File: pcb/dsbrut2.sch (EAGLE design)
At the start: 14 parts, among them IC1 4175D, IC2 74HC125D, IC3 MEGA8-AI

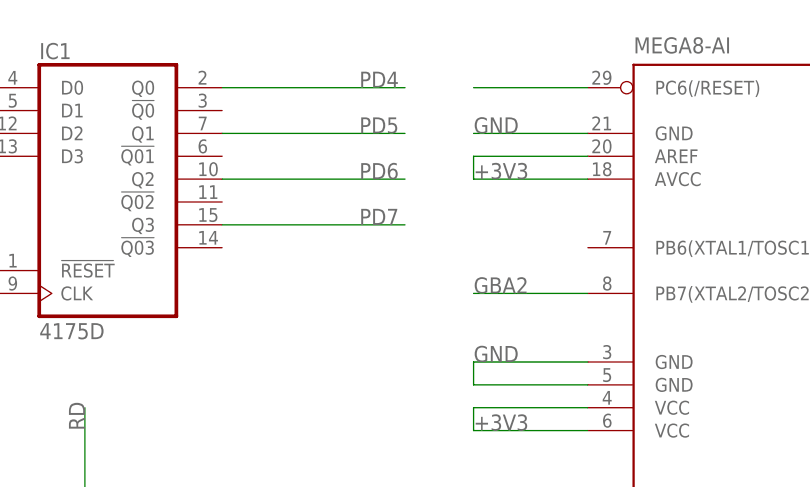
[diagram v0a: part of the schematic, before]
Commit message: added crystal, jumper bridge for gba2
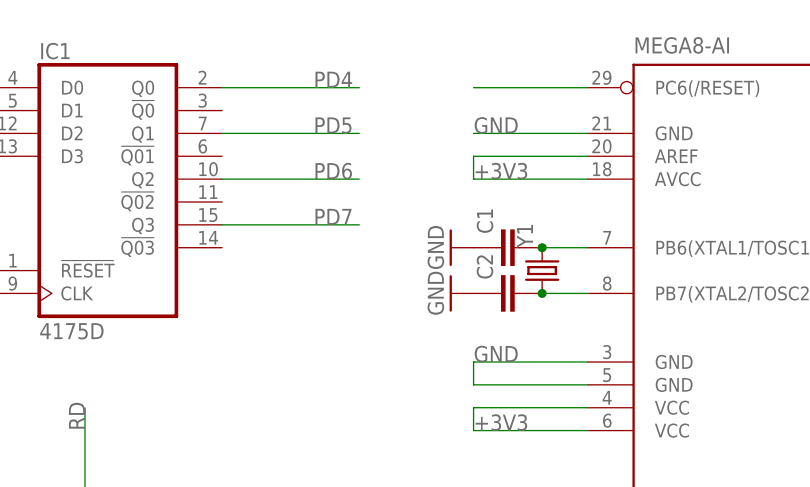
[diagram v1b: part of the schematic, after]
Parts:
- added C1, C2: (no value), rcl:C-EUC0603K
- added Y1: (no value), SparkFun-FreqCtrl:CRYSTAL5X3
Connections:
- new net N$3: C1.2, IC3.PB6(XTAL1/TOSC1), Y1.2
- new net PB7: C2.2, IC3.PB7(XTAL2/TOSC2), Y1.1
- net GBA2: no longer IC3.PB7(XTAL2/TOSC2)
- net GND: now also C1.1, C2.1
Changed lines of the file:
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@@
 <grid distance="0.1" unitdist="inch" unit="inch" style="lines" multiple="1" display="no" altdistance="0.01" altunitdist="inch" altunit="inch"/>
 <layers>
-<layer number="1" name="Top" color="4" fill="1" visible="yes" active="no"/>
-<layer number="16" name="Bottom" color="1" fill="1" visible="yes" active="no"/>
-<layer number="17" name="Pads" color="2" fill="1" visible="yes" active="no"/>
-<layer number="18" name="Vias" color="2" fill="1" visible="yes" active="no"/>
-<layer number="19" name="Unrouted" color="6" fill="1" visible="yes" active="no"/>
-<layer number="20" name="Dimension" color="15" fill="1" visible="yes" active="no"/>
-<layer number="21" name="tPlace" color="7" fill="1" visible="yes" active="no"/>
-<layer number="22" name="bPlace" color="7" fill="1" visible="yes" active="no"/>
-<layer number="23" name="tOrigins" color="15" fill="1" visible="yes" active="no"/>
-<layer number="24" name="bOrigins" color="15" fill="1" visible="yes" active="no"/>
-<layer number="25" name="tNames" color="7" fill="1" visible="yes" active="no"/>
-<layer number="26" name="bNames" color="7" fill="1" visible="yes" active="no"/>
-<layer number="27" name="tValues" color="7" fill="1" visible="yes" active="no"/>
-<layer number="28" name="bValues" color="7" fill="1" visible="yes" active="no"/>
+<layer number="1" name="Top" color="4" fill="1" visible="no" active="no"/>
+<layer number="16" name="Bottom" color="1" fill="1" visible="no" active="no"/>
+<layer number="17" name="Pads" color="2" fill="1" visible="no" active="no"/>
+<layer number="18" name="Vias" color="2" fill="1" visible="no" active="no"/>
+<layer number="19" name="Unrouted" color="6" fill="1" visible="no" active="no"/>
+<layer number="20" name="Dimension" color="15" fill="1" visible="no" active="no"/>
+<layer number="21" name="tPlace" color="7" fill="1" visible="no" active="no"/>
+<layer number="22" name="bPlace" color="7" fill="1" visible="no" active="no"/>
+<layer number="23" name="tOrigins" color="15" fill="1" visible="no" active="no"/>
+<layer number="24" name="bOrigins" color="15" fill="1" visible="no" active="no"/>
+<layer number="25" name="tNames" color="7" fill="1" visible="no" active="no"/>
+<layer number="26" name="bNames" color="7" fill="1" visible="no" active="no"/>
+<layer number="27" name="tValues" color="7" fill="1" visible="no" active="no"/>
+<layer number="28" name="bValues" color="7" fill="1" visible="no" active="no"/>
 <layer number="29" name="tStop" color="7" fill="3" visible="no" active="no"/>
 <layer number="30" name="bStop" color="7" fill="6" visible="no" active="no"/>
@@
 <layer number="35" name="tGlue" color="7" fill="4" visible="no" active="no"/>
 <layer number="36" name="bGlue" color="7" fill="5" visible="no" active="no"/>
-<layer number="37" name="tTest" color="7" fill="1" visible="yes" active="no"/>
-<layer number="38" name="bTest" color="7" fill="1" visible="yes" active="no"/>
+<layer number="37" name="tTest" color="7" fill="1" visible="no" active="no"/>
+<layer number="38" name="bTest" color="7" fill="1" visible="no" active="no"/>
 <layer number="39" name="tKeepout" color="4" fill="11" visible="no" active="no"/>
 <layer number="40" name="bKeepout" color="1" fill="11" visible="no" active="no"/>
@@
 <layer number="44" name="Drills" color="7" fill="1" visible="no" active="no"/>
 <layer number="45" name="Holes" color="7" fill="1" visible="no" active="no"/>
-<layer number="46" name="Milling" color="3" fill="1" visible="yes" active="no"/>
-<layer number="47" name="Measures" color="7" fill="1" visible="yes" active="no"/>
-<layer number="48" name="Document" color="7" fill="1" visible="yes" active="no"/>
-<layer number="49" name="Reference" color="7" fill="1" visible="yes" active="no"/>
-<layer number="50" name="dxf" color="7" fill="1" visible="yes" active="no"/>
-<layer number="51" name="tDocu" color="7" fill="1" visible="yes" active="no"/>
-<layer number="52" name="bDocu" color="7" fill="1" visible="yes" active="no"/>
-<layer number="53" name="tGND_GNDA" color="7" fill="9" visible="yes" active="no"/>
-<layer number="54" name="bGND_GNDA" color="1" fill="9" visible="yes" active="no"/>
-<layer number="56" name="wert" color="7" fill="1" visible="yes" active="no"/>
+<layer number="46" name="Milling" color="3" fill="1" visible="no" active="no"/>
+<layer number="47" name="Measures" color="7" fill="1" visible="no" active="no"/>
+<layer number="48" name="Document" color="7" fill="1" visible="no" active="no"/>
+<layer number="49" name="Reference" color="7" fill="1" visible="no" active="no"/>
+<layer number="50" name="dxf" color="7" fill="1" visible="no" active="no"/>
+<layer number="51" name="tDocu" color="7" fill="1" visible="no" active="no"/>
+<layer number="52" name="bDocu" color="7" fill="1" visible="no" active="no"/>
+<layer number="53" name="tGND_GNDA" color="7" fill="9" visible="no" active="no"/>
+<layer number="54" name="bGND_GNDA" color="1" fill="9" visible="no" active="no"/>
+<layer number="56" name="wert" color="7" fill="1" visible="no" active="no"/>
 <layer number="91" name="Nets" color="2" fill="1" visible="yes" active="yes"/>
 <layer number="92" name="Busses" color="1" fill="1" visible="yes" active="yes"/>
@@
 <part name="F1" library="dp_devices" deviceset="INDUCTOR" device="-L1812" value="F1"/>
 <part name="VDD1" library="supply1" deviceset="VDD" device=""/>
+<part name="Y1" library="SparkFun-FreqCtrl" deviceset="CRYSTAL" device="5X3"/>
+<part name="C1" library="rcl" deviceset="C-EU" device="C0603K"/>
+<part name="C2" library="rcl" deviceset="C-EU" device="C0603K"/>
+<part name="GND2" library="supply1" deviceset="GND" device=""/>
+<part name="GND4" library="supply1" deviceset="GND" device=""/>
 </parts>
 <sheets>
@@
 </instance>
 <instance part="VDD1" gate="G$1" x="226.06" y="58.42" rot="R270"/>
+<instance part="Y1" gate="G$1" x="104.14" y="129.54" rot="R90"/>
+<instance part="C1" gate="G$1" x="99.06" y="132.08" rot="R90"/>
+<instance part="C2" gate="G$1" x="99.06" y="127" rot="R90"/>
+<instance part="GND2" gate="1" x="93.98" y="132.08" rot="R270"/>
+<instance part="GND4" gate="1" x="93.98" y="127" rot="R270"/>
 </instances>
 <busses>
@@
 <pinref part="VSS1" gate="G$1" pin="VSS"/>
 </segment>
+<segment>
+<pinref part="C1" gate="G$1" pin="1"/>
+<pinref part="GND2" gate="1" pin="GND"/>
+</segment>
+<segment>
+<pinref part="C2" gate="G$1" pin="1"/>
+<pinref part="GND4" gate="1" pin="GND"/>
+</segment>
 </net>
 <net name="PD4" class="0">
 <segment>
 <pinref part="IC1" gate="G$1" pin="Q0"/>
-<wire x1="68.58" y1="149.86" x2="88.9" y2="149.86" width="0.1524" layer="91"/>
-<label x="83.82" y="149.86" size="1.778" layer="95"/>
+<wire x1="68.58" y1="149.86" x2="83.82" y2="149.86" width="0.1524" layer="91"/>
+<label x="78.74" y="149.86" size="1.778" layer="95"/>
 </segment>
 <segment>
@@
 <segment>
 <pinref part="IC1" gate="G$1" pin="Q1"/>
-<wire x1="68.58" y1="144.78" x2="88.9" y2="144.78" width="0.1524" layer="91"/>
-<label x="83.82" y="144.78" size="1.778" layer="95"/>
+<wire x1="68.58" y1="144.78" x2="83.82" y2="144.78" width="0.1524" layer="91"/>
+<label x="78.74" y="144.78" size="1.778" layer="95"/>
 </segment>
 <segment>
@@
 <segment>
 <pinref part="IC1" gate="G$1" pin="Q2"/>
-<wire x1="68.58" y1="139.7" x2="88.9" y2="139.7" width="0.1524" layer="91"/>
-<label x="83.82" y="139.7" size="1.778" layer="95"/>
+<wire x1="68.58" y1="139.7" x2="83.82" y2="139.7" width="0.1524" layer="91"/>
+<label x="78.74" y="139.7" size="1.778" layer="95"/>
 </segment>
 <segment>
@@
 <segment>
 <pinref part="IC1" gate="G$1" pin="Q3"/>
-<wire x1="68.58" y1="134.62" x2="88.9" y2="134.62" width="0.1524" layer="91"/>
-<label x="83.82" y="134.62" size="1.778" layer="95"/>
+<wire x1="68.58" y1="134.62" x2="83.82" y2="134.62" width="0.1524" layer="91"/>
+<label x="78.74" y="134.62" size="1.778" layer="95"/>
 </segment>
 <segment>
@@
 </net>
 <net name="GBA2" class="0">
-<segment>
-<pinref part="IC3" gate="G$1" pin="PB7(XTAL2/TOSC2)"/>
-<wire x1="109.22" y1="127" x2="96.52" y2="127" width="0.1524" layer="91"/>
-<label x="96.52" y="127" size="1.778" layer="95"/>
-</segment>
 <segment>
 <pinref part="U$1" gate="G$1" pin="P$2"/>
@@
 </segment>
 </net>
+<net name="PB7" class="0">
+<segment>
+<pinref part="IC3" gate="G$1" pin="PB7(XTAL2/TOSC2)"/>
+<pinref part="Y1" gate="G$1" pin="1"/>
+<wire x1="109.22" y1="127" x2="104.14" y2="127" width="0.1524" layer="91"/>
+<pinref part="C2" gate="G$1" pin="2"/>
+<junction x="104.14" y="127"/>
+</segment>
+</net>
+<net name="N$3" class="0">
+<segment>
+<pinref part="IC3" gate="G$1" pin="PB6(XTAL1/TOSC1)"/>
+<pinref part="Y1" gate="G$1" pin="2"/>
+<wire x1="109.22" y1="132.08" x2="104.14" y2="132.08" width="0.1524" layer="91"/>
+<pinref part="C1" gate="G$1" pin="2"/>
+<junction x="104.14" y="132.08"/>
+</segment>
+</net>

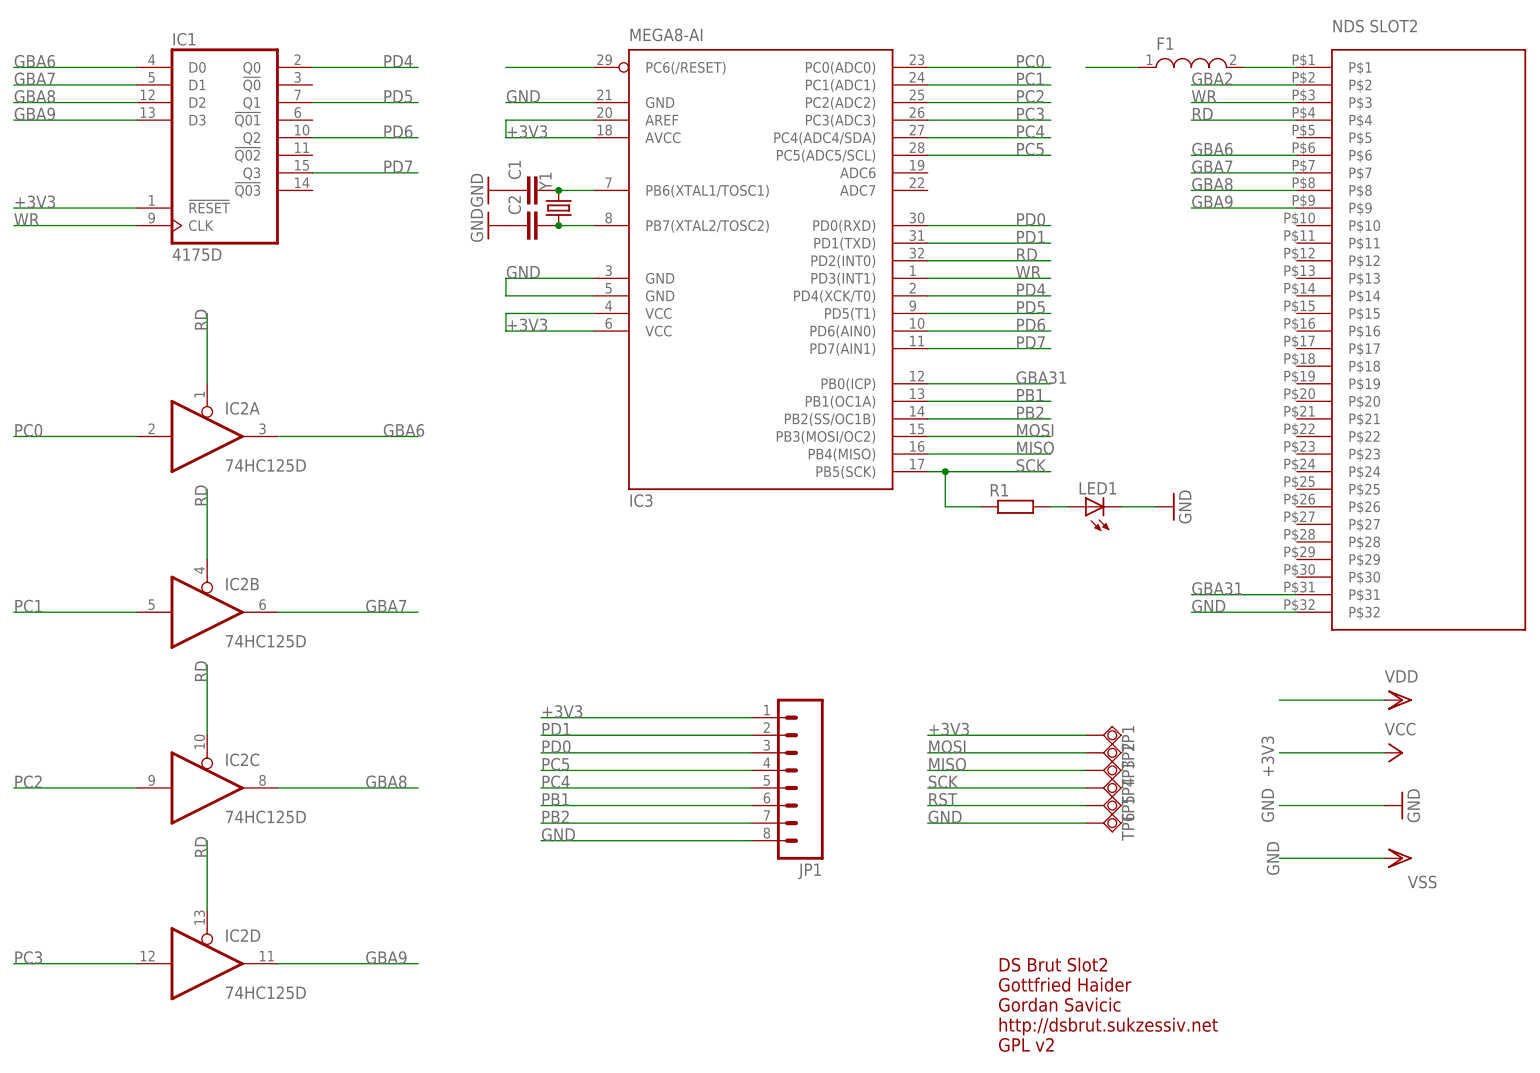
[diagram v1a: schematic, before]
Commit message: cleanup, added our two faces on silkscreen layer
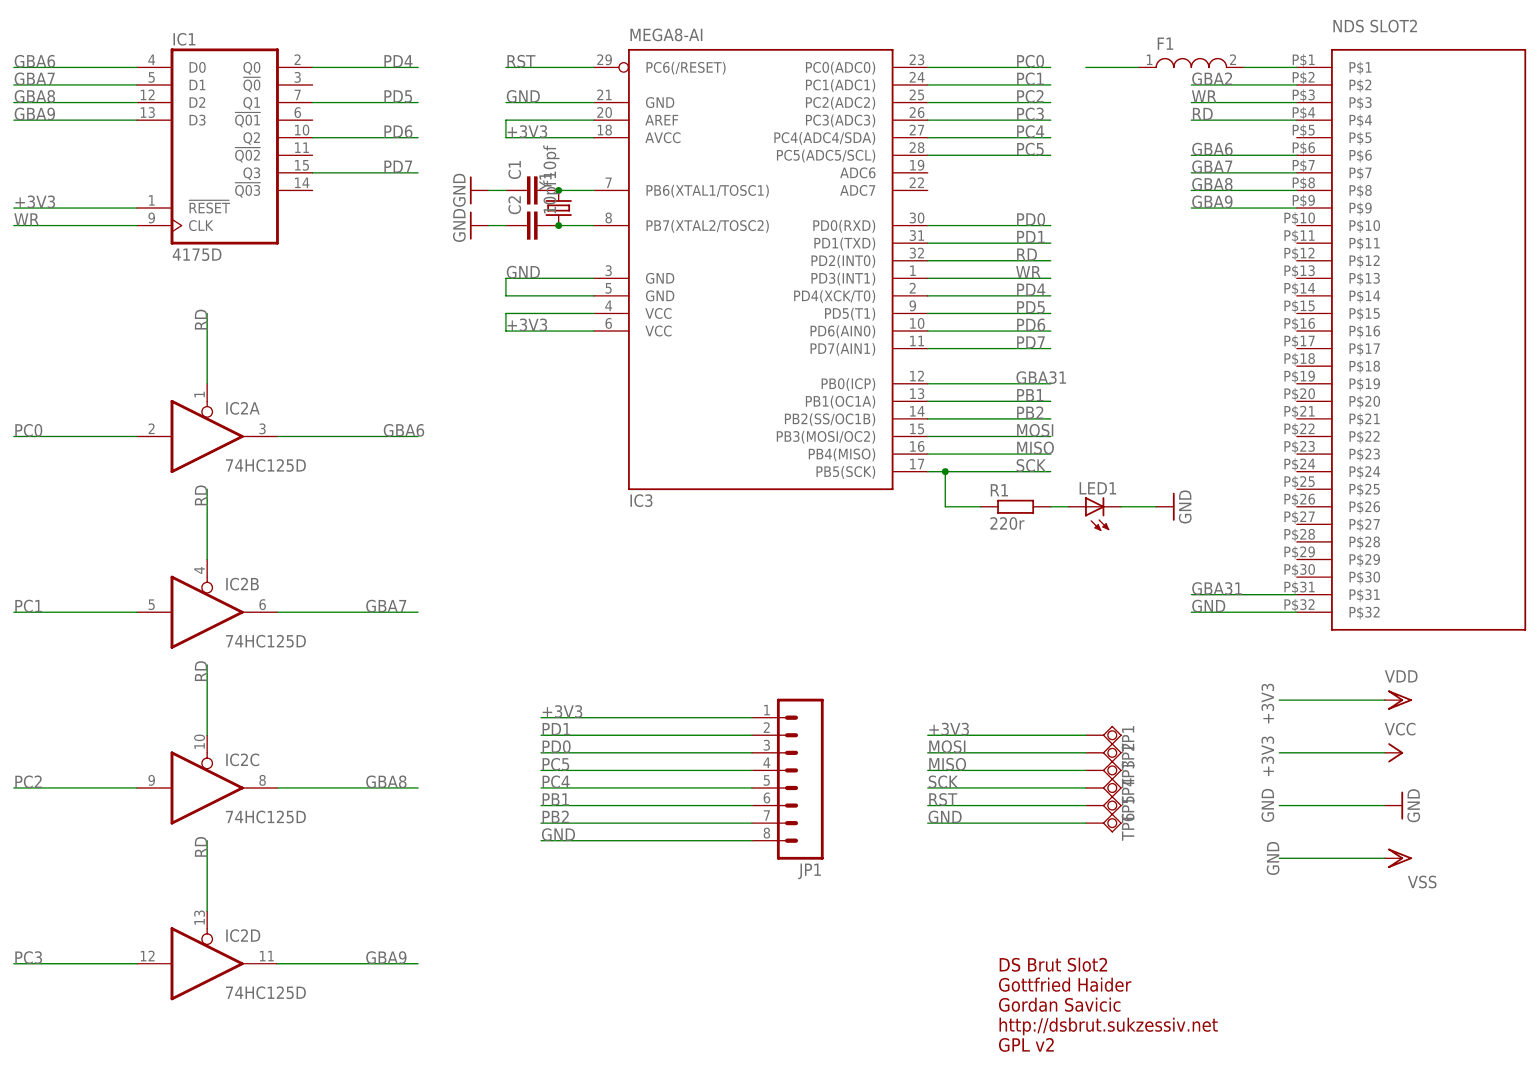
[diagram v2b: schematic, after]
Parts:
- C1, C2: value (none) -> 10pf
- R1: value (none) -> 220r
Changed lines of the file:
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@@
 <part name="LED1" library="SparkFunEagle-6-6-07" deviceset="LED" device="0603"/>
 <part name="GND3" library="supply1" deviceset="GND" device=""/>
-<part name="R1" library="rcl" deviceset="R-EU_" device="M0805"/>
+<part name="R1" library="rcl" deviceset="R-EU_" device="M0805" value="220r"/>
 <part name="VSS1" library="supply1" deviceset="VSS" device=""/>
 <part name="F1" library="dp_devices" deviceset="INDUCTOR" device="-L1812" value="F1"/>
 <part name="VDD1" library="supply1" deviceset="VDD" device=""/>
 <part name="Y1" library="SparkFun-FreqCtrl" deviceset="CRYSTAL" device="5X3"/>
-<part name="C1" library="rcl" deviceset="C-EU" device="C0603K"/>
-<part name="C2" library="rcl" deviceset="C-EU" device="C0603K"/>
+<part name="C1" library="rcl" deviceset="C-EU" device="C0603K" value="10pf"/>
+<part name="C2" library="rcl" deviceset="C-EU" device="C0603K" value="10pf"/>
 <part name="GND2" library="supply1" deviceset="GND" device=""/>
 <part name="GND4" library="supply1" deviceset="GND" device=""/>
@@
 <instance part="C1" gate="G$1" x="99.06" y="132.08" rot="R90"/>
 <instance part="C2" gate="G$1" x="99.06" y="127" rot="R90"/>
-<instance part="GND2" gate="1" x="93.98" y="132.08" rot="R270"/>
-<instance part="GND4" gate="1" x="93.98" y="127" rot="R270"/>
+<instance part="GND2" gate="1" x="91.44" y="132.08" rot="R270"/>
+<instance part="GND4" gate="1" x="91.44" y="127" rot="R270"/>
 </instances>
 <busses>
@@
 <pinref part="VDD1" gate="G$1" pin="VDD"/>
 <wire x1="223.52" y1="58.42" x2="208.28" y2="58.42" width="0.1524" layer="91"/>
+<label x="205.74" y="60.96" size="1.778" layer="95" rot="R270"/>
 </segment>
 </net>
@@
 <pinref part="C1" gate="G$1" pin="1"/>
 <pinref part="GND2" gate="1" pin="GND"/>
+<wire x1="93.98" y1="132.08" x2="96.52" y2="132.08" width="0.1524" layer="91"/>
 </segment>
 <segment>
 <pinref part="C2" gate="G$1" pin="1"/>
 <pinref part="GND4" gate="1" pin="GND"/>
+<wire x1="93.98" y1="127" x2="96.52" y2="127" width="0.1524" layer="91"/>
 </segment>
 </net>
@@
 <pinref part="IC3" gate="G$1" pin="PC6(/RESET)"/>
 <wire x1="109.22" y1="149.86" x2="96.52" y2="149.86" width="0.1524" layer="91"/>
-</segment>
-<segment>
+<label x="96.52" y="149.86" size="1.778" layer="95"/>
+</segment>
+<segment>
